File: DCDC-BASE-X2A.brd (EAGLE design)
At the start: 50 x 70 mm, 7 parts

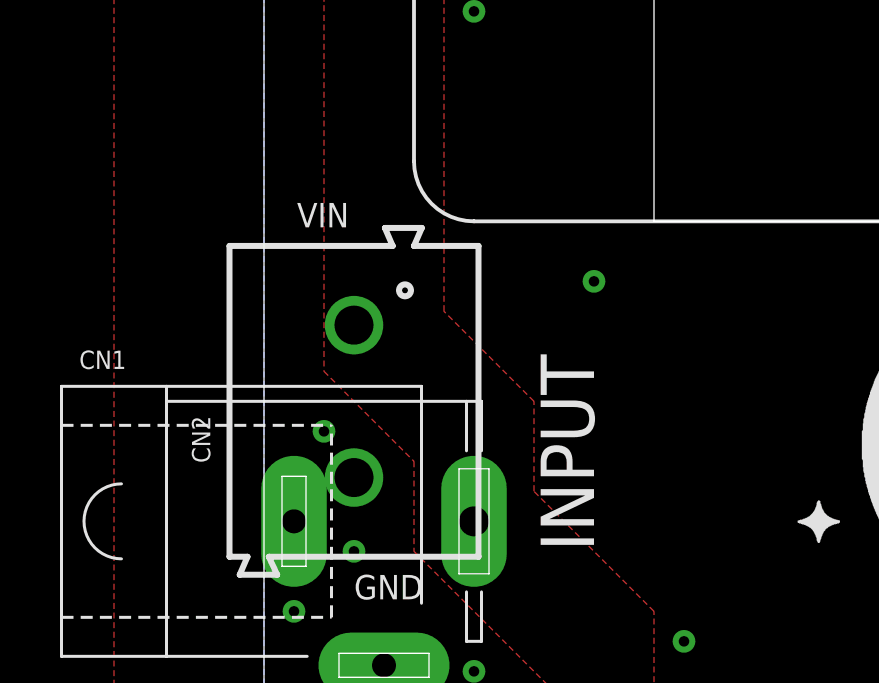
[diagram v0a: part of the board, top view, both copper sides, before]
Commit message: Renamed X2 board to X2A. Generated CAM files. Generated PNG preview. Generated PDF schematics. Updated descriptions.
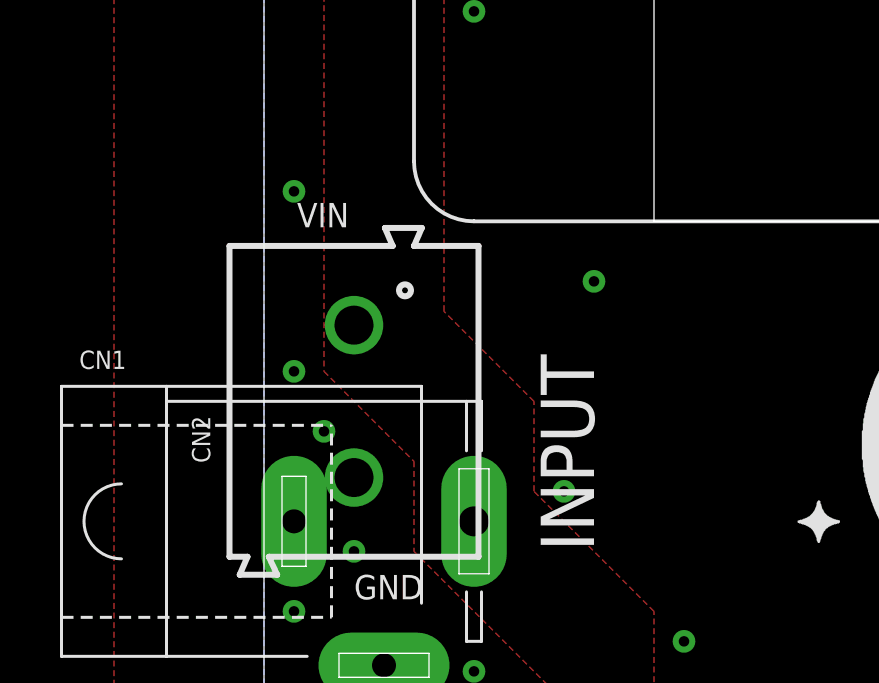
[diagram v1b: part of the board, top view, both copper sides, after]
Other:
- board text added: "DCDC-BASE-X2A-0010"
- board text removed: "DCDC-BASE-X2-0010"
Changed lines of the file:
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@@
 <hole x="47" y="67" drill="3.1"/>
 <hole x="47" y="3" drill="3.1"/>
-<text x="38" y="40" size="1.6764" layer="22" font="vector" ratio="20" rot="MR0">DCDC-BASE-X2-0010</text>
+<text x="38" y="40" size="1.6764" layer="22" font="vector" ratio="20" rot="MR0">DCDC-BASE-X2A-0010</text>
 <text x="3" y="30.4" size="0.8128" layer="21" font="vector">GND</text>
 <text x="42.1" y="34" size="0.8128" layer="21" font="vector" rot="R90">GND</text>
@@
 <via x="47" y="37" extent="1-16" drill="0.35"/>
 <via x="47" y="33" extent="1-16" drill="0.35"/>
+<via x="1" y="44" extent="1-16" drill="0.35"/>
+<via x="1" y="38" extent="1-16" drill="0.35"/>
+<via x="10" y="34" extent="1-16" drill="0.35"/>
 </signal>
 <signal name="VOUT1" airwireshidden="yes">

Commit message: Moved some stuff around on x2 boards. Generated CAM files. Generated PNG preview.
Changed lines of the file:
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@@
 <drawing>
 <settings>
-<setting alwaysvectorfont="yes"/>
+<setting alwaysvectorfont="no"/>
 <setting verticaltext="up"/>
 </settings>
@@
 <vertex x="10" y="22"/>
 <vertex x="6" y="18"/>
-<vertex x="6" y="16"/>
-<vertex x="10" y="16"/>
+<vertex x="6" y="15"/>
+<vertex x="9" y="15"/>
 <vertex x="13" y="19"/>
 <vertex x="13" y="30"/>
@@
 <vertex x="6" y="53"/>
 <vertex x="10" y="57"/>
-<vertex x="10" y="59"/>
-<vertex x="6" y="59"/>
+<vertex x="10" y="60"/>
+<vertex x="7" y="60"/>
 </polygon>
 </signal>
@@
 <contactref element="MOD1" pad="VOUT"/>
 <polygon width="0.3048" layer="1" thermals="no">
-<vertex x="40" y="59"/>
+<vertex x="40" y="60"/>
 <vertex x="40" y="57"/>
 <vertex x="45" y="52"/>
@@
 <vertex x="49" y="39"/>
 <vertex x="49" y="54"/>
-<vertex x="44" y="59"/>
+<vertex x="43" y="60"/>
 </polygon>
 </signal>
@@
 <contactref element="MOD2" pad="VOUT"/>
 <polygon width="0.3048" layer="1" thermals="no">
-<vertex x="40" y="16"/>
+<vertex x="40" y="15"/>
 <vertex x="40" y="19"/>
 <vertex x="45" y="24"/>
@@
 <vertex x="49" y="31"/>
 <vertex x="49" y="21"/>
-<vertex x="44" y="16"/>
+<vertex x="43" y="15"/>
 </polygon>
 </signal>
